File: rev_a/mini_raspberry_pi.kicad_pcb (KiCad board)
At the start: 2 copper layers, 4 parts

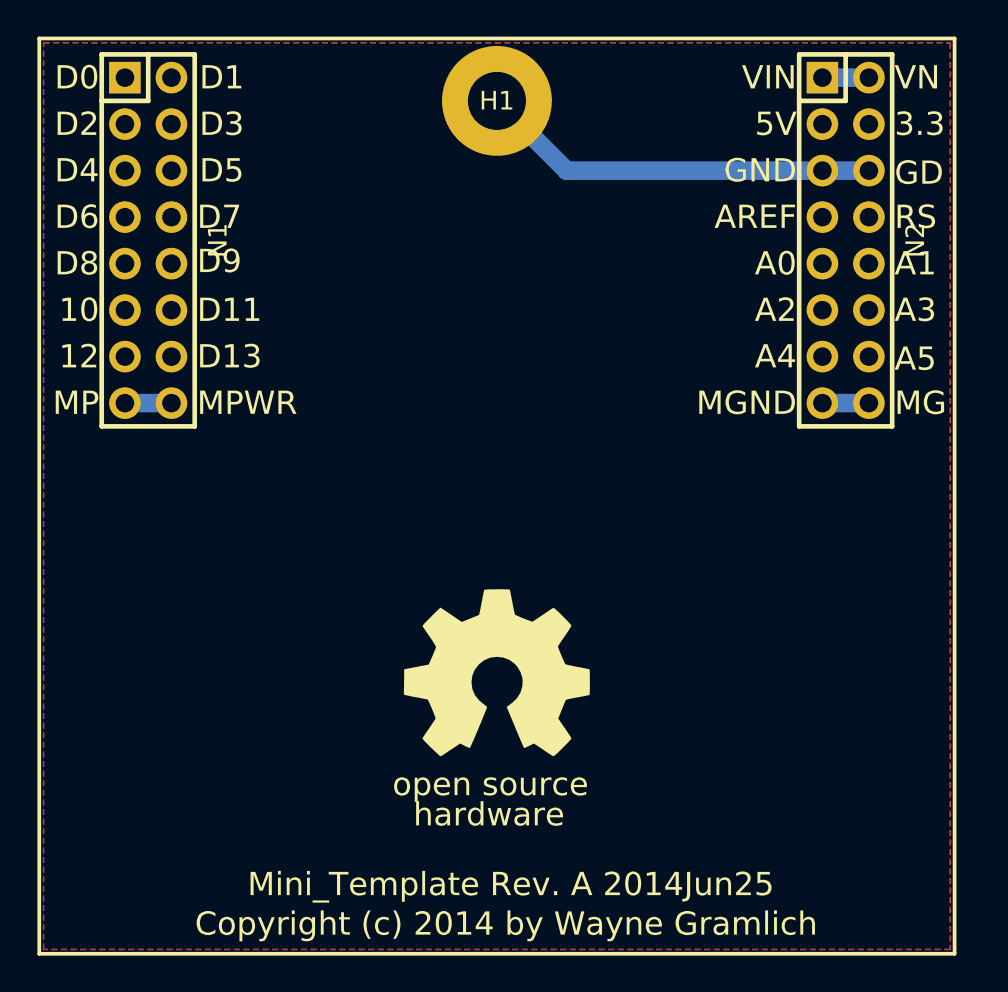
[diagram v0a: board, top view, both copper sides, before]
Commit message: Layed out PCB for Raspberry Pi Mini-Shield
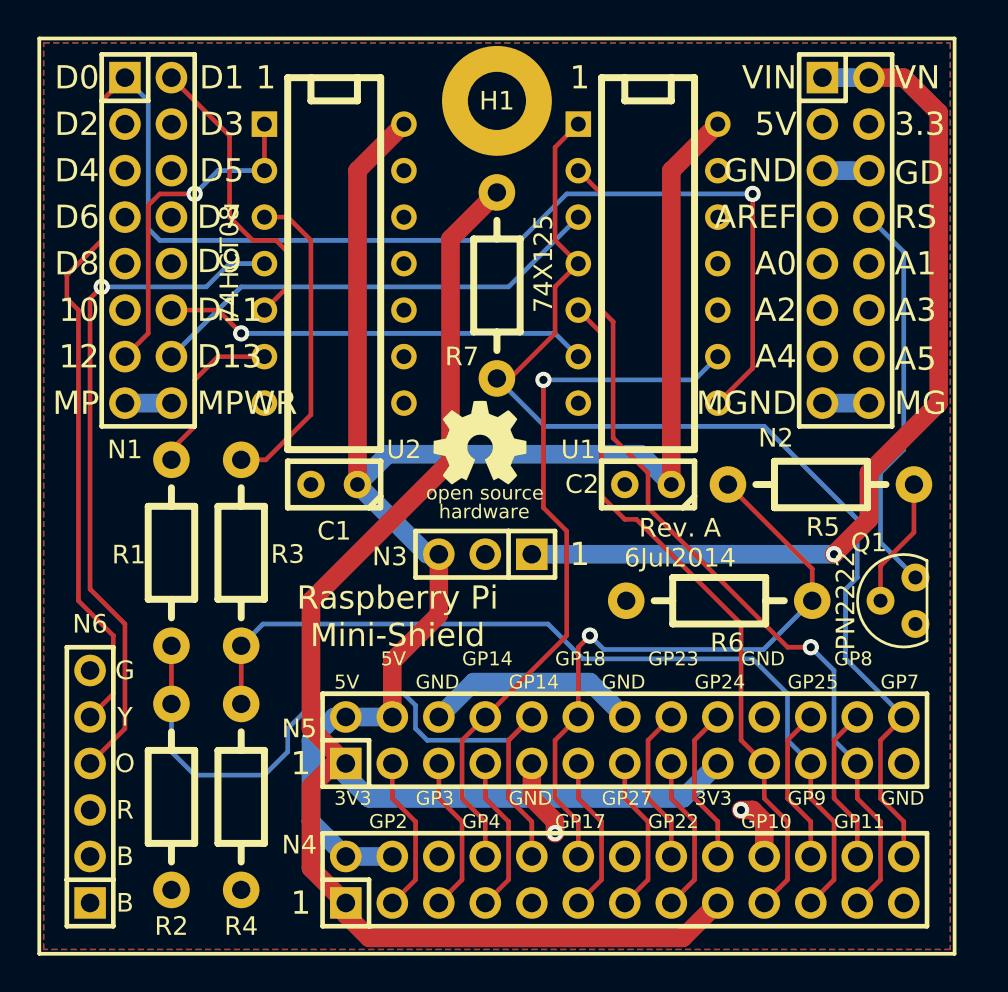
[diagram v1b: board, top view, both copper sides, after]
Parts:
- added C1: .1uF, Mini_Raspberry_Pi_Rev_A:Capacitor3MMDiscRM2.5, F.Cu at (92.7, 127.6)
- added C2: .1uF, Mini_Raspberry_Pi_Rev_A:Capacitor3MMDiscRM2.5, F.Cu at (109.9, 127.6)
- added N3: OKI-78SR-5/1.5-W36-C, Mini_Raspberry_Pi_Rev_A:Pin_Header_Straight_1x03, F.Cu at (101.0, 131.4)
- added N4: RASPI_CONNECTOR, Mini_Raspberry_Pi_Rev_A:Pin_Header_Straight_2x13, F.Cu at (108.6, 149.2)
- added N5: RASPI_HEADER, Mini_Raspberry_Pi_Rev_A:Pin_Header_Straight_2x13, F.Cu at (108.6, 141.6)
- added N6: FTDI_HEADER, Mini_Raspberry_Pi_Rev_A:Pin_Header_Straight_1x06, F.Cu at (79.4, 144.1)
- added Q1: PN2222, Mini_Raspberry_Pi_Rev_A:TO92_123, F.Cu at (123.8, 134.0)
- added R1: 2K2 1%, Mini_Raspberry_Pi_Rev_A:Resistor_Horizontal_RM10mm, F.Cu at (83.8, 131.4)
- added R2: 3K3 1%, Mini_Raspberry_Pi_Rev_A:Resistor_Horizontal_RM10mm, F.Cu at (83.8, 144.8)
- added R3: 2K2 1%, Mini_Raspberry_Pi_Rev_A:Resistor_Horizontal_RM10mm, F.Cu at (87.6, 131.4)
- added R4: 3K3 1%, Mini_Raspberry_Pi_Rev_A:Resistor_Horizontal_RM10mm, F.Cu at (87.6, 144.8)
- added R5: 470, Mini_Raspberry_Pi_Rev_A:Resistor_Horizontal_RM10mm, F.Cu at (119.4, 127.6)
- added R6: 10K, Mini_Raspberry_Pi_Rev_A:Resistor_Horizontal_RM10mm, F.Cu at (113.7, 134.0)
- added R7: 10K, Mini_Raspberry_Pi_Rev_A:Resistor_Horizontal_RM10mm, F.Cu at (101.6, 116.8)
- added U1: 74X125, Mini_Raspberry_Pi_Rev_A:DIP-14__300, F.Cu at (109.9, 115.6)
- added U2: 74HCT08, Mini_Raspberry_Pi_Rev_A:DIP-14__300, F.Cu at (92.7, 115.6)
- G1: footprint Mini_Raspberry_Pi_Rev_A:OSHW_LOGO_400mil -> Mini_Raspberry_Pi_Rev_A:OSHW_LOGO_200mil
- moved G1 12.6 mm to (100.7, 125.3)
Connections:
- net /GND renamed GND
- N1 pad 1: (no net) -> /D0
- N1 pad 12: (no net) -> /D11
- N1 pad 13: (no net) -> /D12
- N1 pad 14: (no net) -> /D13
- N1 pad 2: (no net) -> /D1
- N2 pad 8: (no net) -> /~RESET
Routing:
- net /D0: track 0.00 -> 93.2 mm, vias 0 -> 1
- net /RP_3V3: track 0.00 -> 91.7 mm
- net VCC: track 0.00 -> 90.6 mm, vias 0 -> 1
- net /RP_EN: track 0.00 -> 61.1 mm
- net /RP_SCLK: track 0.00 -> 48.1 mm, vias 0 -> 1
- net /RP_MISO: track 0.00 -> 48.1 mm
- net /VIN: track 2.54 -> 50.1 mm, vias 0 -> 1
- net /RP_RXD: track 0.00 -> 39.6 mm
- net /RP_TXD: track 0.00 -> 39.5 mm, vias 0 -> 1
- net /RP_MOSI: track 0.00 -> 38.7 mm
- net Net-(N6-Pad4): track 0.00 -> 37.3 mm, vias 0 -> 1
- net /RP_RST: track 0.00 -> 35.2 mm, vias 0 -> 1
- net /D13: track 0.00 -> 25.4 mm
- net /D11: track 0.00 -> 23.3 mm, vias 0 -> 1
- net /~RESET: track 0.00 -> 21.8 mm
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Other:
- board text added: "1"
- board text added: "3V3"
- board text added: "B"
- board text added: "Copyright (c) 2014 by Gramlich"
- board text added: "G"
- board text added: "GP10"
- board text added: "GP11"
- board text added: "GP14"
- board text added: "GP17"
- board text added: "GP18"
- board text added: "GP2"
- board text added: "GP22"
- board text added: "GP23"
- board text added: "GP24"
- board text added: "GP25"
- board text added: "GP27"
- board text added: "GP3"
- board text added: "GP4"
- board text added: "GP7"
- board text added: "GP8"
- board text added: "GP9"
- board text added: "O"
- board text added: "R"
- board text added: "Raspberry Pi Mini-Shield"
- board text added: "Rev. A 6Jul2014"
- board text added: "Y"
- board text removed: "Copyright (c) 2014 by Wayne Gramlich"
- board text removed: "Mini_Template Rev. A 2014Jun25"

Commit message: Reworked to improve ground connectivity.
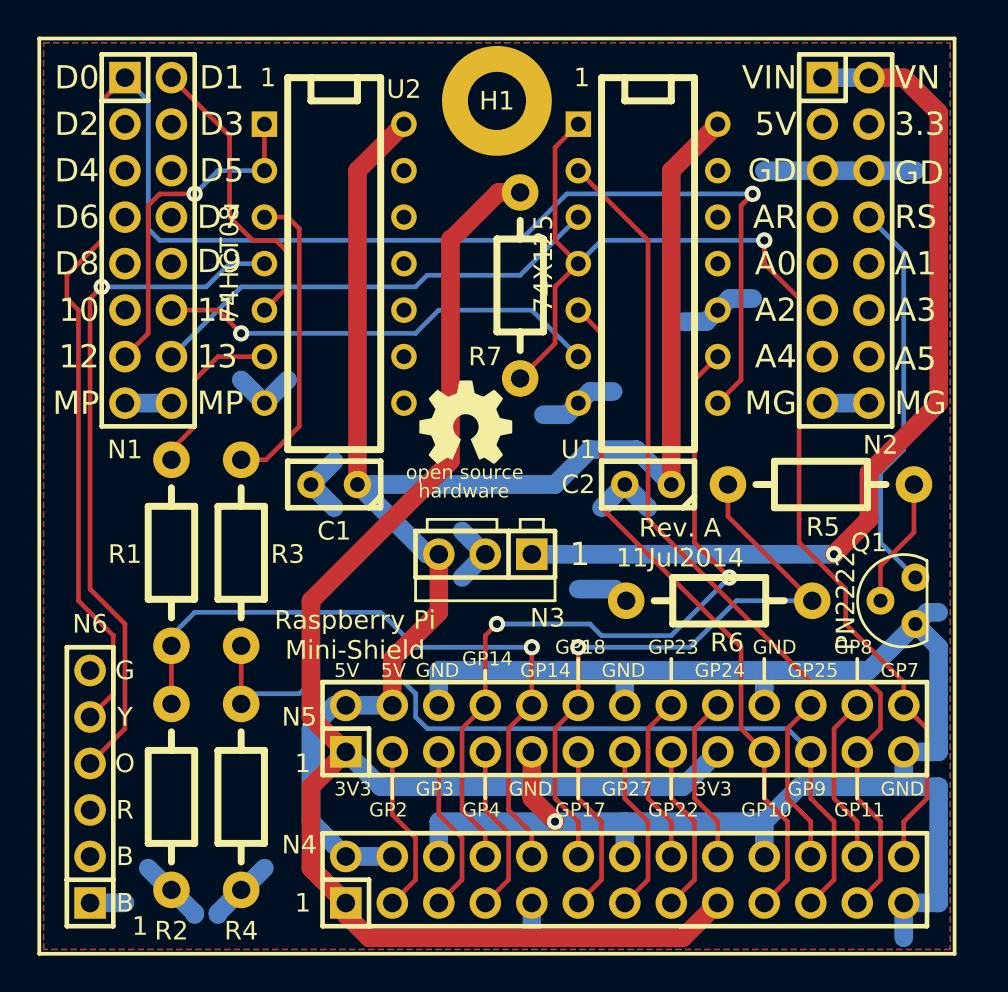
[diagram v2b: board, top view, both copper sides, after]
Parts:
- N3: footprint Mini_Raspberry_Pi_Rev_A:Pin_Header_Straight_1x03 -> Mini_Raspberry_Pi_Rev_A:OKI_DC_TO_DC_CONNECTOR
- moved G1 1.36 mm to (99.9, 124.2)
- moved R7 1.27 mm to (102.9, 116.8)
- moved N5 0.63 mm to (108.6, 141.0)
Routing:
- net GND: track 22.1 -> 139.5 mm, vias 2 -> 1
- net /RP_EN: track 61.1 -> 64.8 mm, vias 0 -> 1
- net /RP_TXD: track 39.5 -> 42.4 mm, vias 1 -> 2
- net /RP_RXD: track 39.6 -> 37.2 mm, vias 0 -> 1
- net /RP_SCLK: track 48.1 -> 50.3 mm, vias 1 -> 0
- net /RP_3V3: track 91.7 -> 93.6 mm
- net /RP_MISO: track 48.1 -> 46.4 mm
- net /D11: track 23.3 -> 24.3 mm
- net /GPIO8: track 8.67 -> 9.31 mm
- net /GPIO23: track 8.67 -> 9.31 mm
- net /GPIO25: track 8.67 -> 9.31 mm
- net /GPIO24: track 8.67 -> 9.31 mm
- net /RP_SDA: track 8.67 -> 9.31 mm
- net /RP_SCL: track 8.67 -> 9.31 mm
- net /GPIO4: track 8.67 -> 9.31 mm
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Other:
- board text added: "11"
- board text added: "13"
- board text added: "AR"
- board text added: "Rev. A 11Jul2014"
- board text removed: "AREF"
- board text removed: "D11"
- board text removed: "D13"
- board text removed: "MGND"
- board text removed: "MPWR"
- board text removed: "Rev. A 6Jul2014"

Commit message: Added edge cuts
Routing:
- net GND: track 139.5 -> 170.9 mm, vias 1 -> 4
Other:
- board outline added: 50 x 50 mm

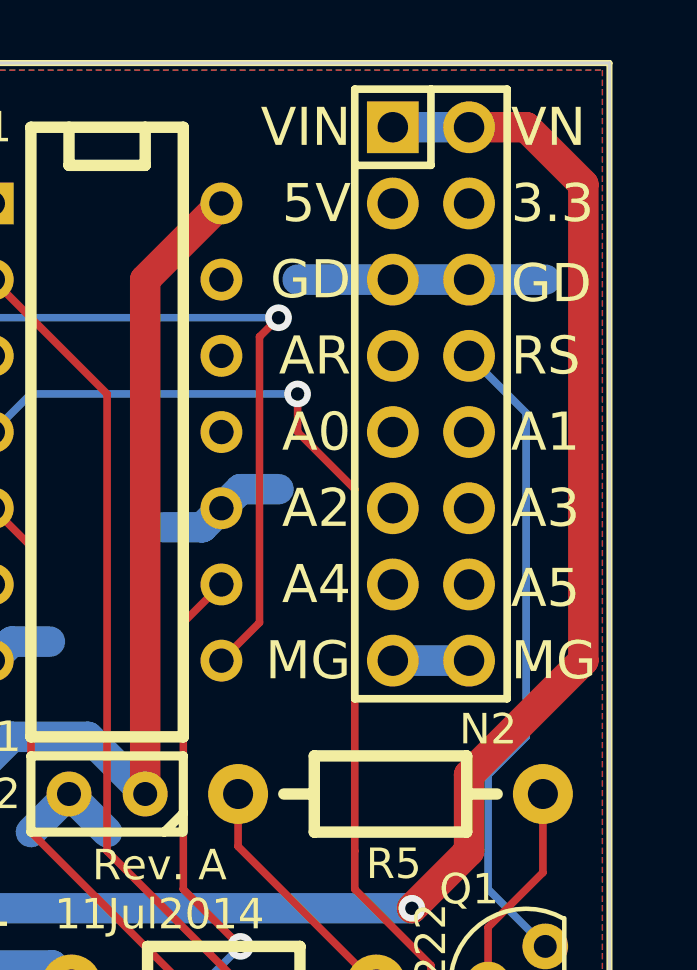
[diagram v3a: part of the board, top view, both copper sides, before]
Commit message: Moved a trace that was too close to PCB edge.
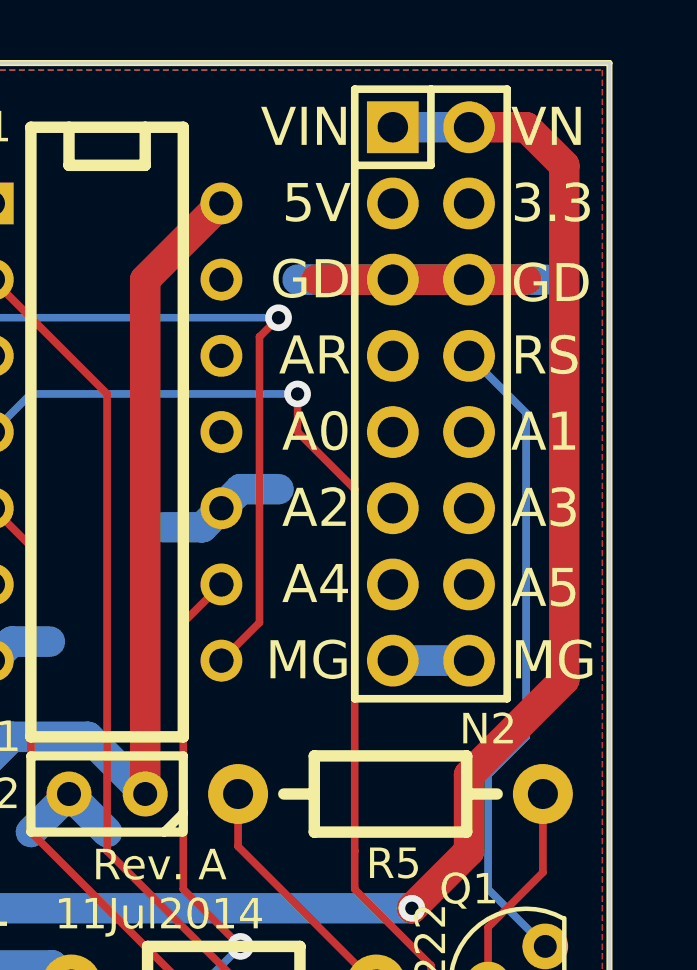
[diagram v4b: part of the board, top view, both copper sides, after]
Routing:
- net GND: track 170.9 -> 177.9 mm
- net /VIN: track 50.1 -> 49.6 mm

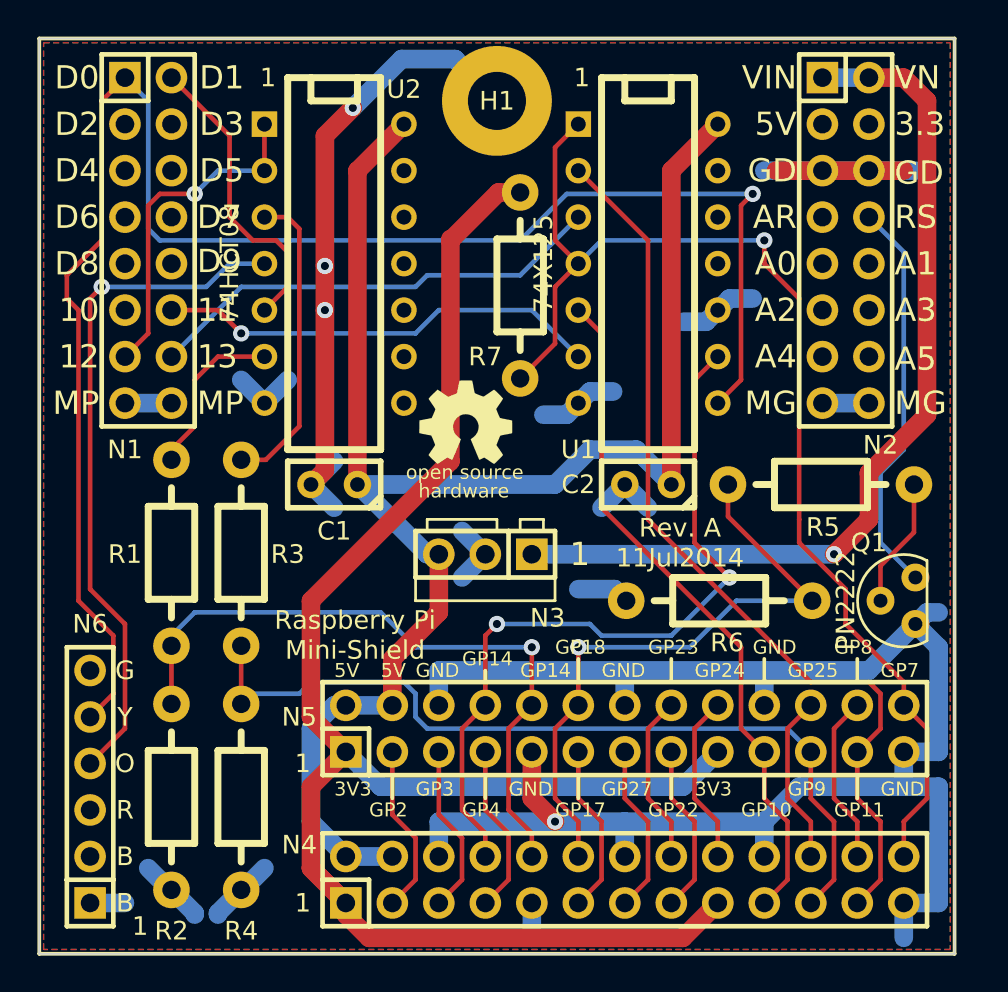
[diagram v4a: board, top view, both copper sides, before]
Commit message: More PCB edge incursions fixed.
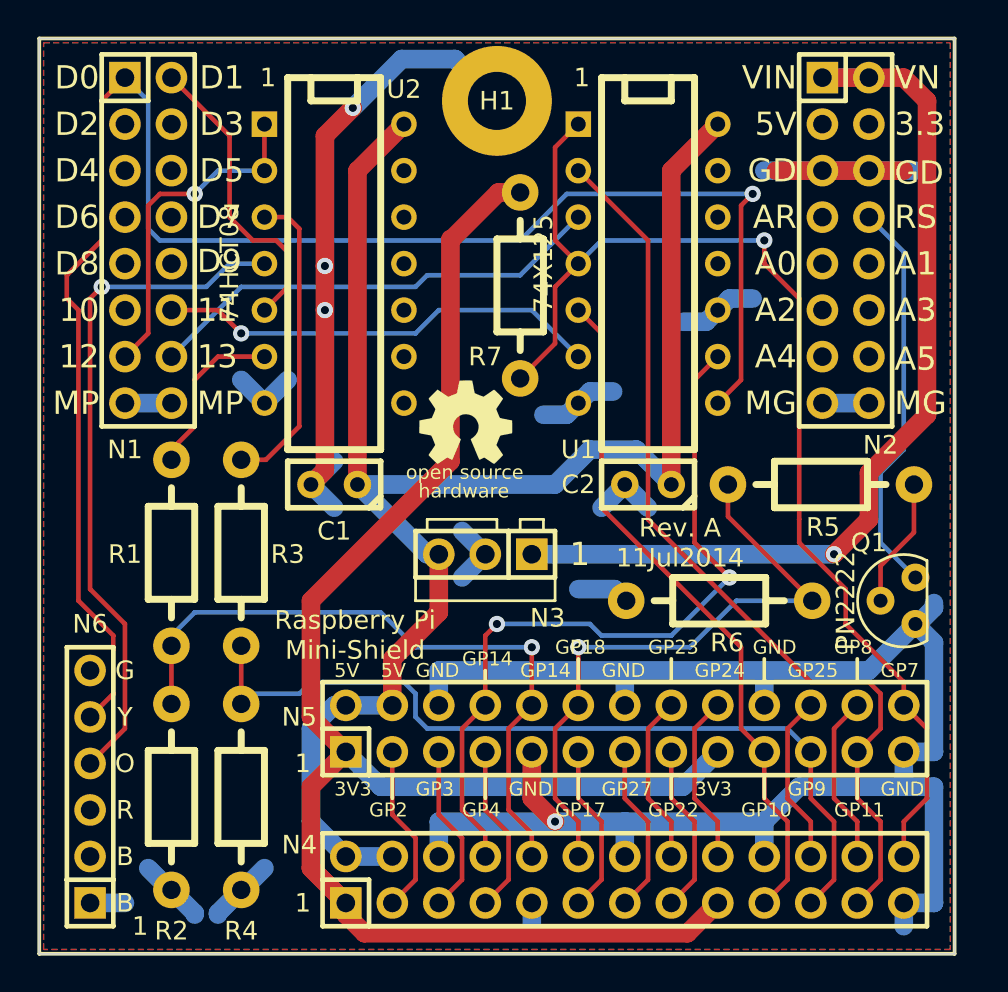
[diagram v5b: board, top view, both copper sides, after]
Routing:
- net /VIN: track 49.6 -> 52.2 mm
- net GND: track 177.9 -> 175.9 mm
